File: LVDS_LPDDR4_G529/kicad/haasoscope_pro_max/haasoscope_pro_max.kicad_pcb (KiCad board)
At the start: 10 copper layers, 200 x 125 mm, 4 parts, among them IC1 ADC12DL500ACF, U1 Ti90G529_Functions, U2 MT53E256M32D2DS-046 IT:B, U3 FT601Q

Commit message: Aligned schematics, sort of
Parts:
- IC1: value ADC12DL500ACF -> ADC12DL500ACF_Aligned
- U1: value Ti90G529_Functions -> MT53D512M16D1DS_Aligned; footprint G529:BGA-529_23x23_19.0x19.0mm -> MT53D512M32D2DS-053 WT_D:IC_MT53D512M16D1DS-046_WT_D
- U2: value MT53E256M32D2DS-046 IT:B -> FT601Q_Aligned; footprint MT53D512M32D2DS-053 WT_D:IC_MT53D512M16D1DS-046_WT_D -> Package_DFN_QFN:QFN-76-1EP_9x9mm_P0.4mm_EP5.81x6.31mm
- U3: value FT601Q -> Ti90G529_Functions; footprint Package_DFN_QFN:QFN-76-1EP_9x9mm_P0.4mm_EP5.81x6.31mm -> G529:BGA-529_23x23_19.0x19.0mm
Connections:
- IC1 pad A16: unconnected-(IC1-DGND_2-PadA16) -> (no net)
- IC1 pad A2: unconnected-(IC1-AGND_2-PadA2) -> (no net)
- IC1 pad A3: unconnected-(IC1-AGND_3-PadA3) -> (no net)
- IC1 pad A6: unconnected-(IC1-AGND_4-PadA6) -> (no net)
- IC1 pad A7: unconnected-(IC1-AGND_5-PadA7) -> (no net)
- IC1 pad B3: unconnected-(IC1-AGND_6-PadB3) -> (no net)
- IC1 pad B4: unconnected-(IC1-AGND_7-PadB4) -> (no net)
- IC1 pad B5: unconnected-(IC1-AGND_8-PadB5) -> (no net)
- IC1 pad B6: unconnected-(IC1-AGND_9-PadB6) -> (no net)
- IC1 pad B7: unconnected-(IC1-AGND_10-PadB7) -> (no net)
- IC1 pad C1: unconnected-(IC1-AGND_11-PadC1) -> (no net)
- IC1 pad C2: unconnected-(IC1-AGND_12-PadC2) -> (no net)
- IC1 pad C3: unconnected-(IC1-AGND_13-PadC3) -> (no net)
- IC1 pad C4: unconnected-(IC1-AGND_14-PadC4) -> (no net)
- IC1 pad C5: unconnected-(IC1-AGND_15-PadC5) -> (no net)
- IC1 pad C6: unconnected-(IC1-AGND_16-PadC6) -> (no net)
- IC1 pad C7: unconnected-(IC1-AGND_17-PadC7) -> (no net)
- IC1 pad D3: unconnected-(IC1-AGND_18-PadD3) -> (no net)
- IC1 pad D4: unconnected-(IC1-AGND_19-PadD4) -> (no net)
- IC1 pad D5: unconnected-(IC1-AGND_20-PadD5) -> (no net)
- IC1 pad D6: unconnected-(IC1-AGND_21-PadD6) -> (no net)
- IC1 pad D7: unconnected-(IC1-DGND_3-PadD7) -> (no net)
- IC1 pad E3: unconnected-(IC1-AGND_22-PadE3) -> (no net)
- IC1 pad E5: unconnected-(IC1-VA11_2-PadE5) -> (no net)
- IC1 pad E6: unconnected-(IC1-VA11_3-PadE6) -> (no net)
- IC1 pad E7: unconnected-(IC1-DGND_4-PadE7) -> (no net)
- IC1 pad F1: unconnected-(IC1-AGND_23-PadF1) -> (no net)
- IC1 pad F2: unconnected-(IC1-AGND_24-PadF2) -> (no net)
- IC1 pad F3: unconnected-(IC1-VA11_4-PadF3) -> (no net)
- IC1 pad F4: unconnected-(IC1-VA11_5-PadF4) -> (no net)
- IC1 pad F5: unconnected-(IC1-VA11_6-PadF5) -> (no net)
- IC1 pad F6: unconnected-(IC1-VA11_7-PadF6) -> (no net)
- IC1 pad F7: unconnected-(IC1-DGND_5-PadF7) -> (no net)
- IC1 pad F8: unconnected-(IC1-VD11_2-PadF8) -> (no net)
- IC1 pad G1: unconnected-(IC1-AGND_25-PadG1) -> (no net)
- IC1 pad G12: unconnected-(IC1-VLVDS_2-PadG12) -> (no net)
- IC1 pad G2: unconnected-(IC1-AGND_26-PadG2) -> (no net)
- IC1 pad G4: unconnected-(IC1-VA19_2-PadG4) -> (no net)
- IC1 pad G5: unconnected-(IC1-VA19_3-PadG5) -> (no net)
- IC1 pad G6: unconnected-(IC1-VA19_4-PadG6) -> (no net)
- IC1 pad G7: unconnected-(IC1-DGND_6-PadG7) -> (no net)
- IC1 pad G8: unconnected-(IC1-VD11_3-PadG8) -> (no net)
- IC1 pad H11: unconnected-(IC1-VLVDS_3-PadH11) -> (no net)
- IC1 pad H12: unconnected-(IC1-VLVDS_4-PadH12) -> (no net)
- IC1 pad H13: unconnected-(IC1-VLVDS_5-PadH13) -> (no net)
- IC1 pad H14: unconnected-(IC1-DGND_9-PadH14) -> (no net)
- IC1 pad H2: unconnected-(IC1-AGND_27-PadH2) -> (no net)
- IC1 pad H3: unconnected-(IC1-VA19_5-PadH3) -> (no net)
- IC1 pad H4: unconnected-(IC1-VA19_6-PadH4) -> (no net)
- IC1 pad H5: unconnected-(IC1-VA19_7-PadH5) -> (no net)
- IC1 pad H6: unconnected-(IC1-VA19_8-PadH6) -> (no net)
- IC1 pad H7: unconnected-(IC1-DGND_7-PadH7) -> (no net)
- IC1 pad H8: unconnected-(IC1-DGND_8-PadH8) -> (no net)
- IC1 pad J11: unconnected-(IC1-VLVDS_6-PadJ11) -> (no net)
- IC1 pad J12: unconnected-(IC1-VLVDS_7-PadJ12) -> (no net)
- IC1 pad J13: unconnected-(IC1-VLVDS_8-PadJ13) -> (no net)
- IC1 pad J14: unconnected-(IC1-DGND_12-PadJ14) -> (no net)
- IC1 pad J2: unconnected-(IC1-AGND_28-PadJ2) -> (no net)
- IC1 pad J3: unconnected-(IC1-VA19_9-PadJ3) -> (no net)
- IC1 pad J4: unconnected-(IC1-VA19_10-PadJ4) -> (no net)
- IC1 pad J5: unconnected-(IC1-VA19_11-PadJ5) -> (no net)
- IC1 pad J6: unconnected-(IC1-VA19_12-PadJ6) -> (no net)
- IC1 pad J7: unconnected-(IC1-DGND_10-PadJ7) -> (no net)
- IC1 pad J8: unconnected-(IC1-DGND_11-PadJ8) -> (no net)
- IC1 pad K1: unconnected-(IC1-AGND_29-PadK1) -> (no net)
- IC1 pad K11: unconnected-(IC1-VLVDS_9-PadK11) -> (no net)
- IC1 pad K12: unconnected-(IC1-VLVDS_10-PadK12) -> (no net)
- IC1 pad K2: unconnected-(IC1-AGND_30-PadK2) -> (no net)
- IC1 pad K3: unconnected-(IC1-VA19_13-PadK3) -> (no net)
- IC1 pad K4: unconnected-(IC1-VA19_14-PadK4) -> (no net)
- IC1 pad K5: unconnected-(IC1-VA19_15-PadK5) -> (no net)
- IC1 pad K6: unconnected-(IC1-VA19_16-PadK6) -> (no net)
- IC1 pad K7: unconnected-(IC1-DGND_13-PadK7) -> (no net)
- IC1 pad K8: unconnected-(IC1-VD11_4-PadK8) -> (no net)
- IC1 pad L1: unconnected-(IC1-AGND_31-PadL1) -> (no net)
- IC1 pad L2: unconnected-(IC1-AGND_32-PadL2) -> (no net)
- IC1 pad L3: unconnected-(IC1-VA11_8-PadL3) -> (no net)
- IC1 pad L4: unconnected-(IC1-VA11_9-PadL4) -> (no net)
- IC1 pad L5: unconnected-(IC1-VA11_10-PadL5) -> (no net)
- IC1 pad L6: unconnected-(IC1-VA11_11-PadL6) -> (no net)
- IC1 pad L7: unconnected-(IC1-DGND_14-PadL7) -> (no net)
- IC1 pad L8: unconnected-(IC1-VD11_5-PadL8) -> (no net)
- IC1 pad M3: unconnected-(IC1-AGND_33-PadM3) -> (no net)
- IC1 pad M4: unconnected-(IC1-VA11_12-PadM4) -> (no net)
- IC1 pad M5: unconnected-(IC1-VA11_13-PadM5) -> (no net)
- IC1 pad M6: unconnected-(IC1-VA11_14-PadM6) -> (no net)
- IC1 pad M7: unconnected-(IC1-DGND_15-PadM7) -> (no net)
- IC1 pad M8: unconnected-(IC1-VD11_6-PadM8) -> (no net)
- IC1 pad N3: unconnected-(IC1-AGND_34-PadN3) -> (no net)
- IC1 pad N4: unconnected-(IC1-AGND_35-PadN4) -> (no net)
- IC1 pad N5: unconnected-(IC1-AGND_36-PadN5) -> (no net)
- IC1 pad N6: unconnected-(IC1-AGND_37-PadN6) -> (no net)
- IC1 pad N7: unconnected-(IC1-DGND_16-PadN7) -> (no net)
- IC1 pad P1: unconnected-(IC1-AGND_38-PadP1) -> (no net)
- IC1 pad P2: unconnected-(IC1-AGND_39-PadP2) -> (no net)
- IC1 pad P3: unconnected-(IC1-AGND_40-PadP3) -> (no net)
- IC1 pad P4: unconnected-(IC1-AGND_41-PadP4) -> (no net)
- IC1 pad P5: unconnected-(IC1-AGND_42-PadP5) -> (no net)
- IC1 pad P6: unconnected-(IC1-AGND_43-PadP6) -> (no net)
- IC1 pad P7: unconnected-(IC1-AGND_44-PadP7) -> (no net)
- IC1 pad R2: unconnected-(IC1-AGND_45-PadR2) -> (no net)
- IC1 pad R3: unconnected-(IC1-AGND_46-PadR3) -> (no net)
- IC1 pad R4: unconnected-(IC1-AGND_47-PadR4) -> (no net)
- IC1 pad R5: unconnected-(IC1-AGND_48-PadR5) -> (no net)
- IC1 pad R6: unconnected-(IC1-AGND_49-PadR6) -> (no net)
- IC1 pad R7: unconnected-(IC1-AGND_50-PadR7) -> (no net)
- IC1 pad T1: unconnected-(IC1-AGND_51-PadT1) -> (no net)
- IC1 pad T15: unconnected-(IC1-DGND_17-PadT15) -> (no net)
- IC1 pad T16: unconnected-(IC1-DGND_18-PadT16) -> (no net)
- IC1 pad T2: unconnected-(IC1-AGND_52-PadT2) -> (no net)
- IC1 pad T3: unconnected-(IC1-AGND_53-PadT3) -> (no net)
- IC1 pad T6: unconnected-(IC1-AGND_54-PadT6) -> (no net)
- IC1 pad T7: unconnected-(IC1-AGND_55-PadT7) -> (no net)
- U1 pad A1: unconnected-(U1N-GND-PadA1) -> (no net)
- U1 pad A10: unconnected-(U1D-ftdi_data[12]-PadA10) -> (no net)
- U1 pad A11: unconnected-(U1D-debugout[11]-PadA11) -> (no net)
- U1 pad A12: unconnected-(U1D-boardout[2]-PadA12) -> (no net)
- U1 pad A2: unconnected-(U1I-lvdsin_trig_N-PadA2) -> (no net)
- U1 pad A4: unconnected-(U1I-GPIOB_P_33_CDI31-PadA4) -> (no net)
- U1 pad A8: unconnected-(U1E-ftdi_data[6]-PadA8) -> (no net)
- U1 pad A9: unconnected-(U1E-debugout[2]-PadA9) -> (no net)
- U1 pad AA1: unconnected-(U1L-DDR_DQ[29]-PadAA1) -> (no net)
- U1 pad AA10: unconnected-(U1L-DDR_DQ[19]-PadAA10) -> (no net)
- U1 pad AA12: unconnected-(U1L-DDR_CKE[0]-PadAA12) -> (no net)
- U1 pad AA3: unconnected-(U1L-DDR_DM[3]-PadAA3) -> (no net)
- U1 pad AA5: unconnected-(U1L-DDR_DQ[27]-PadAA5) -> (no net)
- U1 pad AA8: unconnected-(U1L-DDR_DM[2]-PadAA8) -> (no net)
- U1 pad AB1: unconnected-(U1L-DDR_DQ[28]-PadAB1) -> (no net)
- U1 pad AB10: unconnected-(U1N-VDDQ_PHY-PadAB10) -> (no net)
- U1 pad AB11: unconnected-(U1N-GND-PadAB11) -> (no net)
- U1 pad AB12: unconnected-(U1L-DDR_CK_N-PadAB12) -> (no net)
- U1 pad AB2: unconnected-(U1N-GND-PadAB2) -> (no net)
- U1 pad AB3: unconnected-(U1L-DDR_DQS[3]-PadAB3) -> (no net)
- U1 pad AB4: unconnected-(U1L-DDR_DQ[24]-PadAB4) -> (no net)
- U1 pad AB5: unconnected-(U1N-GND-PadAB5) -> (no net)
- U1 pad AB8: unconnected-(U1L-DDR_DQS[2]-PadAB8) -> (no net)
- U1 pad AB9: unconnected-(U1L-DDR_DQ[16]-PadAB9) -> (no net)
- U1 pad B1: unconnected-(U1I-lvds_rx4_11-PadB1) -> (no net)
- U1 pad B10: unconnected-(U1D-debugout[9]-PadB10) -> (no net)
- U1 pad B12: unconnected-(U1D-ftdi_data[15]-PadB12) -> (no net)
- U1 pad B5: unconnected-(U1M-REF_RES_4A-PadB5) -> (no net)
- U1 pad B8: unconnected-(U1N-VCCIO3C-PadB8) -> (no net)
- U1 pad C1: unconnected-(U1I-lvds_rx4_11_N-PadC1) -> (no net)
- U1 pad C12: unconnected-(U1D-boardout[5]-PadC12) -> (no net)
- U1 pad C5: unconnected-(U1E-ext_clkin-PadC5) -> (no net)
- U1 pad C8: unconnected-(U1E-debugout[0]-PadC8) -> (no net)
- U1 pad D1: unconnected-(U1N-GND-PadD1) -> (no net)
- U1 pad D11: unconnected-(U1D-boardout[0]-PadD11) -> (no net)
- U1 pad D12: unconnected-(U1D-ftdi_data[18]-PadD12) -> (no net)
- U1 pad D2: unconnected-(U1I-lvds_rx4_13-PadD2) -> (no net)
- U1 pad D4: unconnected-(U1N-VCCIO4A-PadD4) -> (no net)
- U1 pad D5: unconnected-(U1I-lvdsin_trig_b-PadD5) -> (no net)
- U1 pad D8: unconnected-(U1E-debugout[1]-PadD8) -> (no net)
- U1 pad D9: unconnected-(U1E-debugout[4]-PadD9) -> (no net)
- U1 pad E1: unconnected-(U1J-lvds_rx3_12-PadE1) -> (no net)
- U1 pad E12: unconnected-(U1D-boardout[3]-PadE12) -> (no net)
- U1 pad E5: unconnected-(U1I-lvdsin_trig_b_N-PadE5) -> (no net)
- U1 pad E8: unconnected-(U1E-ftdi_data[5]-PadE8) -> (no net)
- U1 pad F10: unconnected-(U1D-debugout[8]-PadF10) -> (no net)
- U1 pad F12: unconnected-(U1N-VCCIO3B-PadF12) -> (no net)
- U1 pad F3: unconnected-(U1J-lvds_rx4_5-PadF3) -> (no net)
- U1 pad F5: unconnected-(U1I-exttrigin-PadF5) -> (no net)
- U1 pad F8: unconnected-(U1N-VCCIO33_BR-PadF8) -> (no net)
- U1 pad G1: unconnected-(U1J-lvds_rx_bottom_clkin4-PadG1) -> (no net)
- U1 pad G10: unconnected-(U1N-VCCIO3B-PadG10) -> (no net)
- U1 pad G11: unconnected-(U1D-ftdi_data[14]-PadG11) -> (no net)
- U1 pad G12: unconnected-(U1D-ftdi_data[17]-PadG12) -> (no net)
- U1 pad G3: unconnected-(U1J-lvds_rx4_5_N-PadG3) -> (no net)
- U1 pad G4: unconnected-(U1N-VCCIO4A-PadG4) -> (no net)
- U1 pad G5: unconnected-(U1I-GPIOB_N_34-PadG5) -> (no net)
- U1 pad G8: unconnected-(U1B-ftdi_siwu-PadG8) -> (no net)
- U1 pad G9: unconnected-(U1B-ftdi_resetn-PadG9) -> (no net)
- U1 pad H1: unconnected-(U1N-GND-PadH1) -> (no net)
- U1 pad H12: unconnected-(U1D-boardout[4]-PadH12) -> (no net)
- U1 pad H3: unconnected-(U1J-lvds_rx4_4_N-PadH3) -> (no net)
- U1 pad H5: unconnected-(U1J-lvds_rx4_8-PadH5) -> (no net)
- U1 pad H8: unconnected-(U1B-ftdi_gpio0-PadH8) -> (no net)
- U1 pad J1: unconnected-(U1M-REF_RES_4B-PadJ1) -> (no net)
- U1 pad J10: unconnected-(U1N-GND-PadJ10) -> (no net)
- U1 pad J12: unconnected-(U1N-GND-PadJ12) -> (no net)
- U1 pad J3: unconnected-(U1J-lvds_rx4_2-PadJ3) -> (no net)
- U1 pad J5: unconnected-(U1J-lvds_rx4_8_N-PadJ5) -> (no net)
- U1 pad K10: unconnected-(U1N-VCC-PadK10) -> (no net)
- U1 pad K11: unconnected-(U1N-GND-PadK11) -> (no net)
- U1 pad K12: unconnected-(U1N-VCC-PadK12) -> (no net)
- U1 pad K2: unconnected-(U1N-GND-PadK2) -> (no net)
- U1 pad K3: unconnected-(U1J-lvds_rx4_1_N-PadK3) -> (no net)
- U1 pad K4: unconnected-(U1J-lvds_rx4_7-PadK4) -> (no net)
- U1 pad K5: unconnected-(U1N-GND-PadK5) -> (no net)
- U1 pad K8: unconnected-(U1N-VCCAUX-PadK8) -> (no net)
- U1 pad K9: unconnected-(U1N-GND-PadK9) -> (no net)
- U1 pad N1: unconnected-(U1K-lvds_rx3_8-PadN1) -> (no net)
- U1 pad N10: unconnected-(U1N-GND-PadN10) -> (no net)
- U1 pad N11: unconnected-(U1N-VCC-PadN11) -> (no net)
- U1 pad N12: unconnected-(U1N-GND-PadN12) -> (no net)
- U1 pad N2: unconnected-(U1K-lvds_rx3_8_N-PadN2) -> (no net)
- U1 pad N3: unconnected-(U1K-lvds_rx3_7-PadN3) -> (no net)
- U1 pad N4: unconnected-(U1K-lvds_rx3_9-PadN4) -> (no net)
- U1 pad N5: unconnected-(U1K-lvds_rx3_6-PadN5) -> (no net)
- U1 pad N8: unconnected-(U1N-GND-PadN8) -> (no net)
- U1 pad N9: unconnected-(U1N-VCC-PadN9) -> (no net)
- U1 pad P1: unconnected-(U1K-lvds_rx3_4-PadP1) -> (no net)
- U1 pad P10: unconnected-(U1N-GND-PadP10) -> (no net)
- U1 pad P12: unconnected-(U1N-VDD_PHY-PadP12) -> (no net)
- U1 pad P3: unconnected-(U1K-lvds_rx3_7_N-PadP3) -> (no net)
- U1 pad P5: unconnected-(U1K-lvds_rx3_5-PadP5) -> (no net)
- U1 pad R1: unconnected-(U1K-lvds_rx3_4_N-PadR1) -> (no net)
- U1 pad R12: unconnected-(U1N-GND-PadR12) -> (no net)
- U1 pad R3: unconnected-(U1K-lvds_rx3_2_N-PadR3) -> (no net)
- U1 pad R5: unconnected-(U1K-lvds_rx_bottom_clkin3_N-PadR5) -> (no net)
- U1 pad R8: unconnected-(U1N-VCCAUX-PadR8) -> (no net)
- U1 pad T1: unconnected-(U1N-GND-PadT1) -> (no net)
- U1 pad T10: unconnected-(U1N-VDD_PHY-PadT10) -> (no net)
- U1 pad T12: unconnected-(U1N-VDDQ_CK_PHY-PadT12) -> (no net)
- U1 pad T3: unconnected-(U1A-GPIOL_05_CLK26-PadT3) -> (no net)
- U1 pad T4: unconnected-(U1M-TDO-PadT4) -> (no net)
- U1 pad T5: unconnected-(U1M-TMS-PadT5) -> (no net)
- U1 pad T8: unconnected-(U1N-VCC-PadT8) -> (no net)
- U1 pad T9: unconnected-(U1N-VDD_PHY-PadT9) -> (no net)
- U1 pad U1: unconnected-(U1A-LED[0]-PadU1) -> (no net)
- U1 pad U10: unconnected-(U1N-VDDQX_PHY-PadU10) -> (no net)
- U1 pad U12: unconnected-(U1N-VDDPLL_MCB_TOP_PHY-PadU12) -> (no net)
- U1 pad U3: unconnected-(U1A-GPIOL_02-PadU3) -> (no net)
- U1 pad U5: unconnected-(U1M-TCK-PadU5) -> (no net)
- U1 pad U8: unconnected-(U1N-VCC-PadU8) -> (no net)
- U1 pad V1: unconnected-(U1A-GPIOL_06_CLK27-PadV1) -> (no net)
- U1 pad V12: unconnected-(U1N-VDDQX_PHY-PadV12) -> (no net)
- U1 pad V5: unconnected-(U1A-GPIOL_21-PadV5) -> (no net)
- U1 pad V8: unconnected-(U1L-DDR_CAL-PadV8) -> (no net)
- U1 pad W1: unconnected-(U1A-LED[1]-PadW1) -> (no net)
- U1 pad W10: (no net) -> unconnected-(U1B-DQS1_t_B-PadW10)
- U1 pad W12: unconnected-(U1N-VDDQ_PHY-PadW12) -> (no net)
- U1 pad W2: unconnected-(U1A-fan_out-PadW2) -> (no net)
- U1 pad W4: unconnected-(U1A-main_pllin-PadW4) -> (no net)
- U1 pad W5: unconnected-(U1A-GPIOL_03_CLK24-PadW5) -> (no net)
- U1 pad W8: unconnected-(U1L-DDR_A[4]-PadW8) -> (no net)
- U1 pad W9: unconnected-(U1L-DDR_A[3]-PadW9) -> (no net)
- U1 pad Y1: unconnected-(U1N-VDDQ_PHY-PadY1) -> (no net)
- U1 pad Y12: unconnected-(U1N-GND-PadY12) -> (no net)
- U1 pad Y5: unconnected-(U1N-VDDQ_PHY-PadY5) -> (no net)
- U1 pad Y8: unconnected-(U1N-GND-PadY8) -> (no net)
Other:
- board text added: "ADC12DL"
- board text added: "FT601"
- board text added: "MT53D512M32D2DS"
- board text added: "Ti90G529"

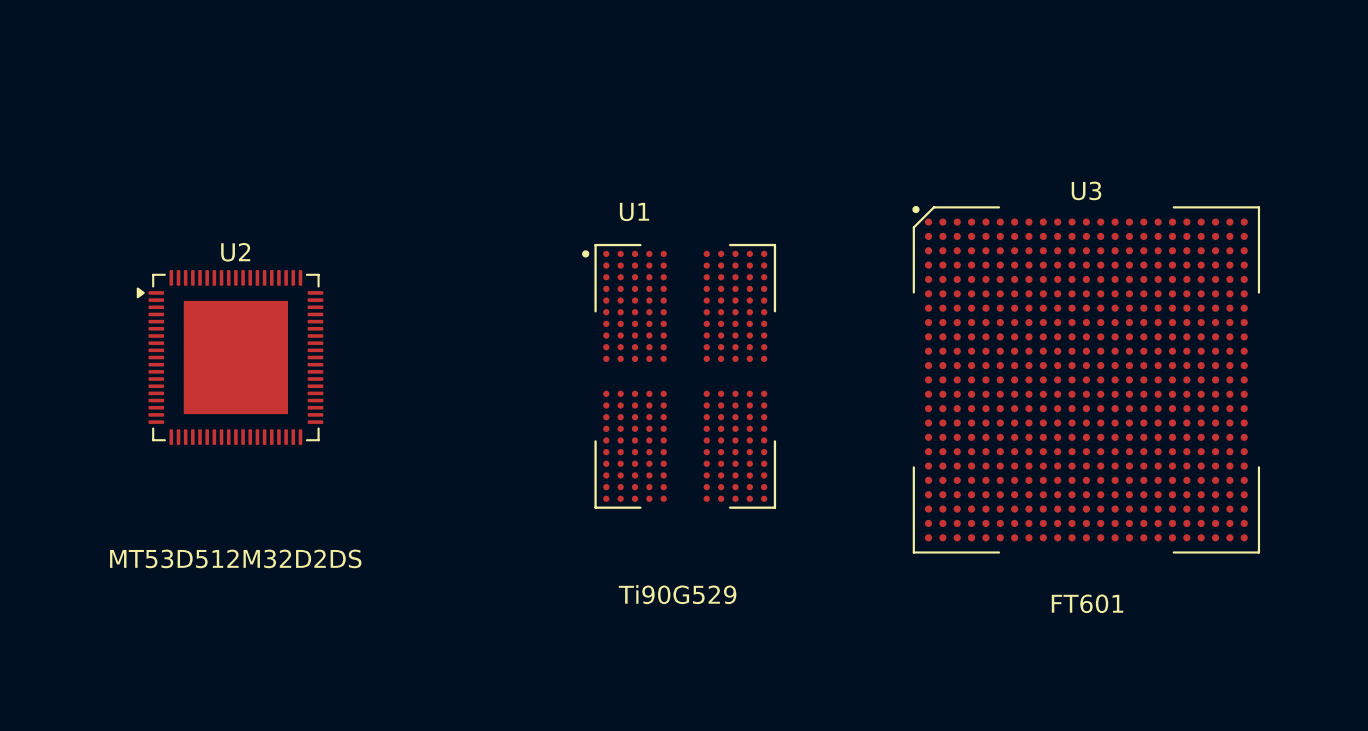
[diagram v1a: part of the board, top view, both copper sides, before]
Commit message: Aligned schematics, connected some components
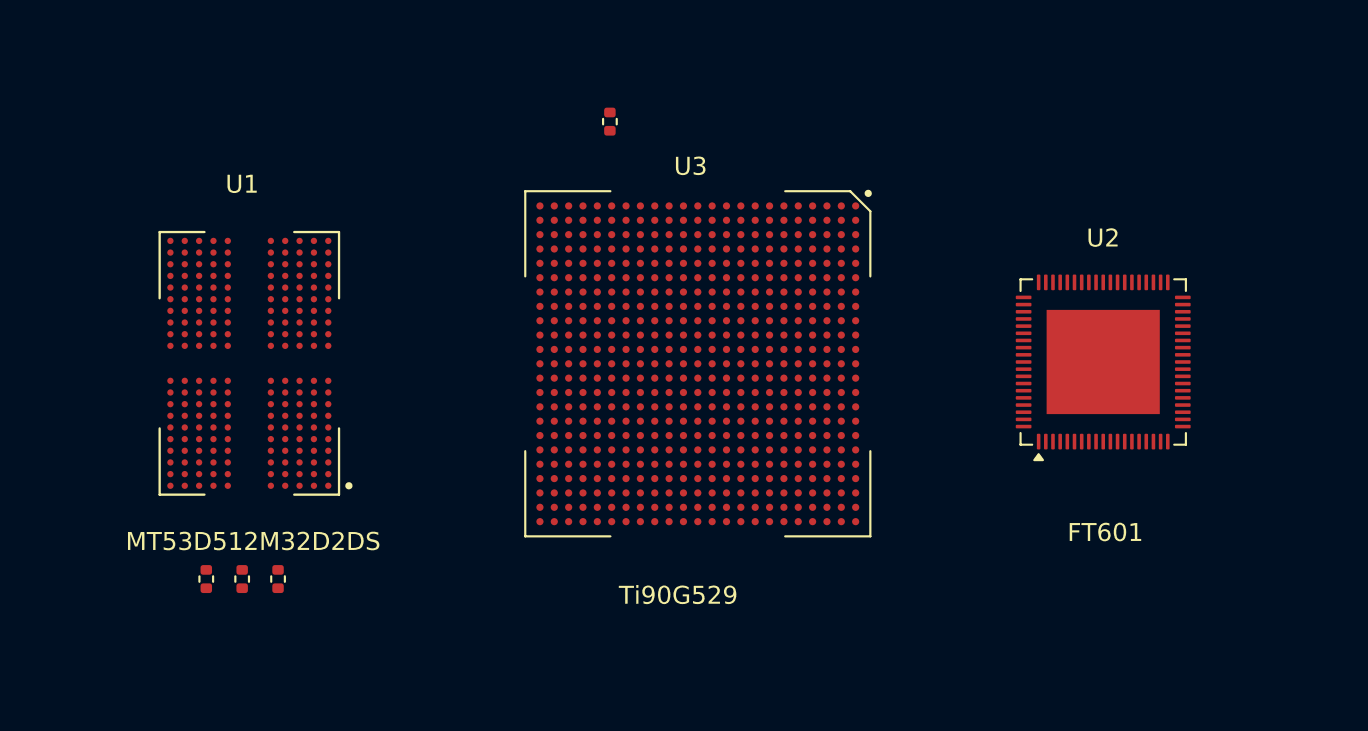
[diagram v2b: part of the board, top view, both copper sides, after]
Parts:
- added R1: 240, Resistor_SMD:R_0402_1005Metric, F.Cu at (190.5, 89.5)
- added R2: 240, Resistor_SMD:R_0402_1005Metric, F.Cu at (172.0, 115.0)
- added R3: 240, Resistor_SMD:R_0402_1005Metric, F.Cu at (170.0, 115.0)
- added R4: 240, Resistor_SMD:R_0402_1005Metric, F.Cu at (168.0, 115.0)
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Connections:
- IC1 pad A10: unconnected-(IC1A-DA0--PadA10) -> Net-(IC1A-DA0-)
- IC1 pad A11: unconnected-(IC1A-DA6+-PadA11) -> Net-(IC1A-DA6+)
- IC1 pad A12: unconnected-(IC1A-DA6--PadA12) -> Net-(IC1A-DA6-)
- IC1 pad A13: unconnected-(IC1A-DC0+-PadA13) -> Net-(IC1A-DC0+)
- IC1 pad A14: unconnected-(IC1A-DC0--PadA14) -> Net-(IC1A-DC0-)
- IC1 pad A16: (no net) -> unconnected-(IC1F-DGND_2-PadA16)
- IC1 pad A2: (no net) -> unconnected-(IC1F-AGND_2-PadA2)
- IC1 pad A3: (no net) -> unconnected-(IC1F-AGND_3-PadA3)
- IC1 pad A6: (no net) -> unconnected-(IC1F-AGND_4-PadA6)
- IC1 pad A7: (no net) -> unconnected-(IC1F-AGND_5-PadA7)
- IC1 pad A9: unconnected-(IC1A-DA0+-PadA9) -> Net-(IC1A-DA0+)
- IC1 pad B10: unconnected-(IC1A-DA1--PadB10) -> Net-(IC1A-DA1-)
- IC1 pad B11: unconnected-(IC1A-DA7+-PadB11) -> Net-(IC1A-DA7+)
- IC1 pad B12: unconnected-(IC1A-DA7--PadB12) -> Net-(IC1A-DA7-)
- IC1 pad B13: unconnected-(IC1A-DC1+-PadB13) -> Net-(IC1A-DC1+)
- IC1 pad B14: unconnected-(IC1A-DC1--PadB14) -> Net-(IC1A-DC1-)
- IC1 pad B15: unconnected-(IC1A-DC7+-PadB15) -> Net-(IC1A-DC7+)
- IC1 pad B16: unconnected-(IC1A-DC7--PadB16) -> Net-(IC1A-DC7-)
- IC1 pad B3: (no net) -> unconnected-(IC1F-AGND_6-PadB3)
- IC1 pad B4: (no net) -> unconnected-(IC1F-AGND_7-PadB4)
- IC1 pad B5: (no net) -> unconnected-(IC1F-AGND_8-PadB5)
- IC1 pad B6: (no net) -> unconnected-(IC1F-AGND_9-PadB6)
- IC1 pad B7: (no net) -> unconnected-(IC1F-AGND_10-PadB7)
- IC1 pad B9: unconnected-(IC1A-DA1+-PadB9) -> Net-(IC1A-DA1+)
- IC1 pad C1: (no net) -> unconnected-(IC1F-AGND_11-PadC1)
- IC1 pad C10: unconnected-(IC1A-DA2--PadC10) -> Net-(IC1A-DA2-)
- IC1 pad C11: unconnected-(IC1A-DA8+-PadC11) -> Net-(IC1A-DA8+)
- IC1 pad C12: unconnected-(IC1A-DA8--PadC12) -> Net-(IC1A-DA8-)
- IC1 pad C13: unconnected-(IC1A-DC2+-PadC13) -> Net-(IC1A-DC2+)
- IC1 pad C14: unconnected-(IC1A-DC2--PadC14) -> Net-(IC1A-DC2-)
- IC1 pad C15: unconnected-(IC1A-DC8+-PadC15) -> Net-(IC1A-DC8+)
- IC1 pad C16: unconnected-(IC1A-DC8--PadC16) -> Net-(IC1A-DC8-)
- IC1 pad C2: (no net) -> unconnected-(IC1F-AGND_12-PadC2)
- IC1 pad C3: (no net) -> unconnected-(IC1F-AGND_13-PadC3)
- IC1 pad C4: (no net) -> unconnected-(IC1F-AGND_14-PadC4)
- IC1 pad C5: (no net) -> unconnected-(IC1F-AGND_15-PadC5)
- IC1 pad C6: (no net) -> unconnected-(IC1F-AGND_16-PadC6)
- IC1 pad C7: (no net) -> unconnected-(IC1F-AGND_17-PadC7)
- IC1 pad C9: unconnected-(IC1A-DA2+-PadC9) -> Net-(IC1A-DA2+)
- IC1 pad D10: unconnected-(IC1A-DA3--PadD10) -> Net-(IC1A-DA3-)
- IC1 pad D11: unconnected-(IC1A-DA9+-PadD11) -> Net-(IC1A-DA9+)
- IC1 pad D12: unconnected-(IC1A-DA9--PadD12) -> Net-(IC1A-DA9-)
- IC1 pad D13: unconnected-(IC1A-DC3+-PadD13) -> Net-(IC1A-DC3+)
- IC1 pad D14: unconnected-(IC1A-DC3--PadD14) -> Net-(IC1A-DC3-)
- IC1 pad D15: unconnected-(IC1A-DC9+-PadD15) -> Net-(IC1A-DC9+)
- IC1 pad D16: unconnected-(IC1A-DC9--PadD16) -> Net-(IC1A-DC9-)
- IC1 pad D3: (no net) -> unconnected-(IC1F-AGND_18-PadD3)
- IC1 pad D4: (no net) -> unconnected-(IC1F-AGND_19-PadD4)
- IC1 pad D5: (no net) -> unconnected-(IC1F-AGND_20-PadD5)
- IC1 pad D6: (no net) -> unconnected-(IC1F-AGND_21-PadD6)
- IC1 pad D7: (no net) -> unconnected-(IC1F-DGND_3-PadD7)
- IC1 pad D9: unconnected-(IC1A-DA3+-PadD9) -> Net-(IC1A-DA3+)
- IC1 pad E10: unconnected-(IC1A-DA4--PadE10) -> Net-(IC1A-DA4-)
- IC1 pad E11: unconnected-(IC1A-DA10+-PadE11) -> Net-(IC1A-DA10+)
- IC1 pad E12: unconnected-(IC1A-DA10--PadE12) -> Net-(IC1A-DA10-)
- IC1 pad E13: unconnected-(IC1A-DC4+-PadE13) -> Net-(IC1A-DC4+)
- IC1 pad E14: unconnected-(IC1A-DC4--PadE14) -> Net-(IC1A-DC4-)
- IC1 pad E15: unconnected-(IC1A-DC10+-PadE15) -> Net-(IC1A-DC10+)
- IC1 pad E16: unconnected-(IC1A-DC10--PadE16) -> Net-(IC1A-DC10-)
- IC1 pad E3: (no net) -> unconnected-(IC1F-AGND_22-PadE3)
- IC1 pad E5: (no net) -> unconnected-(IC1F-VA11_2-PadE5)
- IC1 pad E6: (no net) -> unconnected-(IC1F-VA11_3-PadE6)
- IC1 pad E7: (no net) -> unconnected-(IC1F-DGND_4-PadE7)
- IC1 pad E9: unconnected-(IC1A-DA4+-PadE9) -> Net-(IC1A-DA4+)
- IC1 pad F1: (no net) -> unconnected-(IC1F-AGND_23-PadF1)
- IC1 pad F10: unconnected-(IC1A-DA5--PadF10) -> Net-(IC1A-DA5-)
- IC1 pad F11: unconnected-(IC1A-DA11+-PadF11) -> Net-(IC1A-DA11+)
- IC1 pad F12: unconnected-(IC1A-DA11--PadF12) -> Net-(IC1A-DA11-)
- IC1 pad F13: unconnected-(IC1A-DC5+-PadF13) -> Net-(IC1A-DC5+)
- IC1 pad F14: unconnected-(IC1A-DC5--PadF14) -> Net-(IC1A-DC5-)
- IC1 pad F15: unconnected-(IC1A-DC11+-PadF15) -> Net-(IC1A-DC11+)
- IC1 pad F16: unconnected-(IC1A-DC11--PadF16) -> Net-(IC1A-DC11-)
- IC1 pad F2: (no net) -> unconnected-(IC1F-AGND_24-PadF2)
- IC1 pad F3: (no net) -> unconnected-(IC1F-VA11_4-PadF3)
- IC1 pad F4: (no net) -> unconnected-(IC1F-VA11_5-PadF4)
- IC1 pad F5: (no net) -> unconnected-(IC1F-VA11_6-PadF5)
- IC1 pad F6: (no net) -> unconnected-(IC1F-VA11_7-PadF6)
- IC1 pad F7: (no net) -> unconnected-(IC1F-DGND_5-PadF7)
- IC1 pad F8: (no net) -> unconnected-(IC1F-VD11_2-PadF8)
- IC1 pad F9: unconnected-(IC1A-DA5+-PadF9) -> Net-(IC1A-DA5+)
- IC1 pad G1: (no net) -> unconnected-(IC1F-AGND_25-PadG1)
- IC1 pad G10: unconnected-(IC1A-DACLK--PadG10) -> Net-(IC1C-DACLK-)
- IC1 pad G12: (no net) -> unconnected-(IC1F-VLVDS_2-PadG12)
- IC1 pad G13: unconnected-(IC1A-DC6+-PadG13) -> Net-(IC1A-DC6+)
- IC1 pad G14: unconnected-(IC1A-DC6--PadG14) -> Net-(IC1A-DC6-)
- IC1 pad G15: unconnected-(IC1A-DCCLK+-PadG15) -> Net-(IC1C-DCCLK+)
- IC1 pad G16: unconnected-(IC1A-DCCLK--PadG16) -> Net-(IC1C-DCCLK-)
- IC1 pad G2: (no net) -> unconnected-(IC1F-AGND_26-PadG2)
- IC1 pad G4: (no net) -> unconnected-(IC1F-VA19_2-PadG4)
- IC1 pad G5: (no net) -> unconnected-(IC1F-VA19_3-PadG5)
- IC1 pad G6: (no net) -> unconnected-(IC1F-VA19_4-PadG6)
- IC1 pad G7: (no net) -> unconnected-(IC1F-DGND_6-PadG7)
- IC1 pad G8: (no net) -> unconnected-(IC1F-VD11_3-PadG8)
- IC1 pad G9: unconnected-(IC1A-DACLK+-PadG9) -> Net-(IC1C-DACLK+)
- IC1 pad H10: unconnected-(IC1A-DASTR--PadH10) -> Net-(IC1A-DASTR-)
- IC1 pad H11: (no net) -> unconnected-(IC1F-VLVDS_3-PadH11)
- IC1 pad H12: (no net) -> unconnected-(IC1F-VLVDS_4-PadH12)
- IC1 pad H13: (no net) -> unconnected-(IC1F-VLVDS_5-PadH13)
- IC1 pad H14: (no net) -> unconnected-(IC1F-DGND_9-PadH14)
- IC1 pad H15: unconnected-(IC1A-DCSTR+-PadH15) -> Net-(IC1A-DCSTR+)
- IC1 pad H16: unconnected-(IC1A-DCSTR--PadH16) -> Net-(IC1A-DCSTR-)
- IC1 pad H2: (no net) -> unconnected-(IC1F-AGND_27-PadH2)
- IC1 pad H3: (no net) -> unconnected-(IC1F-VA19_5-PadH3)
- IC1 pad H4: (no net) -> unconnected-(IC1F-VA19_6-PadH4)
- IC1 pad H5: (no net) -> unconnected-(IC1F-VA19_7-PadH5)
- IC1 pad H6: (no net) -> unconnected-(IC1F-VA19_8-PadH6)
- IC1 pad H7: (no net) -> unconnected-(IC1F-DGND_7-PadH7)
- IC1 pad H8: (no net) -> unconnected-(IC1F-DGND_8-PadH8)
- IC1 pad H9: unconnected-(IC1A-DASTR+-PadH9) -> Net-(IC1A-DASTR+)
- IC1 pad J10: unconnected-(IC1B-DBSTR--PadJ10) -> Net-(IC1B-DBSTR-)
- IC1 pad J11: (no net) -> unconnected-(IC1F-VLVDS_6-PadJ11)
- IC1 pad J12: (no net) -> unconnected-(IC1F-VLVDS_7-PadJ12)
- IC1 pad J13: (no net) -> unconnected-(IC1F-VLVDS_8-PadJ13)
- IC1 pad J14: (no net) -> unconnected-(IC1F-DGND_12-PadJ14)
- IC1 pad J15: unconnected-(IC1B-DDSTR+-PadJ15) -> Net-(IC1B-DDSTR+)
- IC1 pad J16: unconnected-(IC1B-DDSTR--PadJ16) -> Net-(IC1B-DDSTR-)
- IC1 pad J2: (no net) -> unconnected-(IC1F-AGND_28-PadJ2)
- IC1 pad J3: (no net) -> unconnected-(IC1F-VA19_9-PadJ3)
- IC1 pad J4: (no net) -> unconnected-(IC1F-VA19_10-PadJ4)
- IC1 pad J5: (no net) -> unconnected-(IC1F-VA19_11-PadJ5)
- IC1 pad J6: (no net) -> unconnected-(IC1F-VA19_12-PadJ6)
- IC1 pad J7: (no net) -> unconnected-(IC1F-DGND_10-PadJ7)
- IC1 pad J8: (no net) -> unconnected-(IC1F-DGND_11-PadJ8)
- IC1 pad J9: unconnected-(IC1B-DBSTR+-PadJ9) -> Net-(IC1B-DBSTR+)
- IC1 pad K1: (no net) -> unconnected-(IC1F-AGND_29-PadK1)
- IC1 pad K10: unconnected-(IC1B-DBCLK--PadK10) -> Net-(IC1C-DBCLK-)
- IC1 pad K11: (no net) -> unconnected-(IC1F-VLVDS_9-PadK11)
- IC1 pad K12: (no net) -> unconnected-(IC1F-VLVDS_10-PadK12)
- IC1 pad K13: unconnected-(IC1B-DD6+-PadK13) -> Net-(IC1B-DD6+)
- IC1 pad K14: unconnected-(IC1B-DD6--PadK14) -> Net-(IC1B-DD6-)
- IC1 pad K15: unconnected-(IC1B-DDCLK+-PadK15) -> Net-(IC1C-DDCLK+)
- IC1 pad K16: unconnected-(IC1B-DDCLK--PadK16) -> Net-(IC1C-DDCLK-)
- IC1 pad K2: (no net) -> unconnected-(IC1F-AGND_30-PadK2)
- IC1 pad K3: (no net) -> unconnected-(IC1F-VA19_13-PadK3)
- IC1 pad K4: (no net) -> unconnected-(IC1F-VA19_14-PadK4)
- IC1 pad K5: (no net) -> unconnected-(IC1F-VA19_15-PadK5)
- IC1 pad K6: (no net) -> unconnected-(IC1F-VA19_16-PadK6)
- IC1 pad K7: (no net) -> unconnected-(IC1F-DGND_13-PadK7)
- IC1 pad K8: (no net) -> unconnected-(IC1F-VD11_4-PadK8)
- IC1 pad K9: unconnected-(IC1B-DBCLK+-PadK9) -> Net-(IC1C-DBCLK+)
- IC1 pad L1: (no net) -> unconnected-(IC1F-AGND_31-PadL1)
- IC1 pad L10: unconnected-(IC1B-DB5--PadL10) -> Net-(IC1B-DB5-)
- IC1 pad L11: unconnected-(IC1B-DB11+-PadL11) -> Net-(IC1B-DB11+)
- IC1 pad L12: unconnected-(IC1B-DB11--PadL12) -> Net-(IC1B-DB11-)
- IC1 pad L13: unconnected-(IC1B-DD5+-PadL13) -> Net-(IC1B-DD5+)
- IC1 pad L14: unconnected-(IC1B-DD5--PadL14) -> Net-(IC1B-DD5-)
- IC1 pad L15: unconnected-(IC1B-DD11+-PadL15) -> Net-(IC1B-DD11+)
- IC1 pad L16: unconnected-(IC1B-DD11--PadL16) -> Net-(IC1B-DD11-)
- IC1 pad L2: (no net) -> unconnected-(IC1F-AGND_32-PadL2)
- IC1 pad L3: (no net) -> unconnected-(IC1F-VA11_8-PadL3)
- IC1 pad L4: (no net) -> unconnected-(IC1F-VA11_9-PadL4)
- IC1 pad L5: (no net) -> unconnected-(IC1F-VA11_10-PadL5)
- IC1 pad L6: (no net) -> unconnected-(IC1F-VA11_11-PadL6)
- IC1 pad L7: (no net) -> unconnected-(IC1F-DGND_14-PadL7)
- IC1 pad L8: (no net) -> unconnected-(IC1F-VD11_5-PadL8)
- IC1 pad L9: unconnected-(IC1B-DB5+-PadL9) -> Net-(IC1B-DB5+)
- IC1 pad M10: unconnected-(IC1B-DB4--PadM10) -> Net-(IC1B-DB4-)
- IC1 pad M11: unconnected-(IC1B-DB10+-PadM11) -> Net-(IC1B-DB10+)
- IC1 pad M12: unconnected-(IC1B-DB10--PadM12) -> Net-(IC1B-DB10-)
- IC1 pad M13: unconnected-(IC1B-DD4+-PadM13) -> Net-(IC1B-DD4+)
- IC1 pad M14: unconnected-(IC1B-DD4--PadM14) -> Net-(IC1B-DD4-)
- IC1 pad M15: unconnected-(IC1B-DD10+-PadM15) -> Net-(IC1B-DD10+)
- IC1 pad M16: unconnected-(IC1B-DD10--PadM16) -> Net-(IC1B-DD10-)
- IC1 pad M3: (no net) -> unconnected-(IC1F-AGND_33-PadM3)
- IC1 pad M4: (no net) -> unconnected-(IC1F-VA11_12-PadM4)
- IC1 pad M5: (no net) -> unconnected-(IC1F-VA11_13-PadM5)
- IC1 pad M6: (no net) -> unconnected-(IC1F-VA11_14-PadM6)
- IC1 pad M7: (no net) -> unconnected-(IC1F-DGND_15-PadM7)
- IC1 pad M8: (no net) -> unconnected-(IC1F-VD11_6-PadM8)
- IC1 pad M9: unconnected-(IC1B-DB4+-PadM9) -> Net-(IC1B-DB4+)
- IC1 pad N10: unconnected-(IC1B-DB3--PadN10) -> Net-(IC1B-DB3-)
- IC1 pad N11: unconnected-(IC1B-DB9+-PadN11) -> Net-(IC1B-DB9+)
- IC1 pad N12: unconnected-(IC1B-DB9--PadN12) -> Net-(IC1B-DB9-)
- IC1 pad N13: unconnected-(IC1B-DD3+-PadN13) -> Net-(IC1B-DD3+)
- IC1 pad N14: unconnected-(IC1B-DD3--PadN14) -> Net-(IC1B-DD3-)
- IC1 pad N15: unconnected-(IC1B-DD9+-PadN15) -> Net-(IC1B-DD9+)
- IC1 pad N16: unconnected-(IC1B-DD9--PadN16) -> Net-(IC1B-DD9-)
- IC1 pad N3: (no net) -> unconnected-(IC1F-AGND_34-PadN3)
- IC1 pad N4: (no net) -> unconnected-(IC1F-AGND_35-PadN4)
- IC1 pad N5: (no net) -> unconnected-(IC1F-AGND_36-PadN5)
- IC1 pad N6: (no net) -> unconnected-(IC1F-AGND_37-PadN6)
- IC1 pad N7: (no net) -> unconnected-(IC1F-DGND_16-PadN7)
- IC1 pad N9: unconnected-(IC1B-DB3+-PadN9) -> Net-(IC1B-DB3+)
- IC1 pad P1: (no net) -> unconnected-(IC1F-AGND_38-PadP1)
- IC1 pad P10: unconnected-(IC1B-DB2--PadP10) -> Net-(IC1B-DB2-)
- IC1 pad P11: unconnected-(IC1B-DB8+-PadP11) -> Net-(IC1B-DB8+)
- IC1 pad P12: unconnected-(IC1B-DB8--PadP12) -> Net-(IC1B-DB8-)
- IC1 pad P13: unconnected-(IC1B-DD2+-PadP13) -> Net-(IC1B-DD2+)
- IC1 pad P14: unconnected-(IC1B-DD2--PadP14) -> Net-(IC1B-DD2-)
- IC1 pad P15: unconnected-(IC1B-DD8+-PadP15) -> Net-(IC1B-DD8+)
- IC1 pad P16: unconnected-(IC1B-DD8--PadP16) -> Net-(IC1B-DD8-)
- IC1 pad P2: (no net) -> unconnected-(IC1F-AGND_39-PadP2)
- IC1 pad P3: (no net) -> unconnected-(IC1F-AGND_40-PadP3)
- IC1 pad P4: (no net) -> unconnected-(IC1F-AGND_41-PadP4)
- IC1 pad P5: (no net) -> unconnected-(IC1F-AGND_42-PadP5)
- IC1 pad P6: (no net) -> unconnected-(IC1F-AGND_43-PadP6)
- IC1 pad P7: (no net) -> unconnected-(IC1F-AGND_44-PadP7)
- IC1 pad P9: unconnected-(IC1B-DB2+-PadP9) -> Net-(IC1B-DB2+)
- IC1 pad R10: unconnected-(IC1B-DB1--PadR10) -> Net-(IC1B-DB1-)
- IC1 pad R11: unconnected-(IC1B-DB7+-PadR11) -> Net-(IC1B-DB7+)
- IC1 pad R12: unconnected-(IC1B-DB7--PadR12) -> Net-(IC1B-DB7-)
- IC1 pad R13: unconnected-(IC1B-DD1+-PadR13) -> Net-(IC1B-DD1+)
- IC1 pad R14: unconnected-(IC1B-DD1--PadR14) -> Net-(IC1B-DD1-)
- IC1 pad R15: unconnected-(IC1B-DD7+-PadR15) -> Net-(IC1B-DD7+)
- IC1 pad R16: unconnected-(IC1B-DD7--PadR16) -> Net-(IC1B-DD7-)
- IC1 pad R2: (no net) -> unconnected-(IC1F-AGND_45-PadR2)
- IC1 pad R3: (no net) -> unconnected-(IC1F-AGND_46-PadR3)
- IC1 pad R4: (no net) -> unconnected-(IC1F-AGND_47-PadR4)
- IC1 pad R5: (no net) -> unconnected-(IC1F-AGND_48-PadR5)
- IC1 pad R6: (no net) -> unconnected-(IC1F-AGND_49-PadR6)
- IC1 pad R7: (no net) -> unconnected-(IC1F-AGND_50-PadR7)
- IC1 pad R9: unconnected-(IC1B-DB1+-PadR9) -> Net-(IC1B-DB1+)
- IC1 pad T1: (no net) -> unconnected-(IC1F-AGND_51-PadT1)
- IC1 pad T10: unconnected-(IC1B-DB0--PadT10) -> Net-(IC1B-DB0-)
- IC1 pad T11: unconnected-(IC1B-DB6+-PadT11) -> Net-(IC1B-DB6+)
- IC1 pad T12: unconnected-(IC1B-DB6--PadT12) -> Net-(IC1B-DB6-)
- IC1 pad T13: unconnected-(IC1B-DD0+-PadT13) -> Net-(IC1B-DD0+)
- IC1 pad T14: unconnected-(IC1B-DD0--PadT14) -> Net-(IC1B-DD0-)
- IC1 pad T15: (no net) -> unconnected-(IC1F-DGND_17-PadT15)
- IC1 pad T16: (no net) -> unconnected-(IC1F-DGND_18-PadT16)
- IC1 pad T2: (no net) -> unconnected-(IC1F-AGND_52-PadT2)
- IC1 pad T3: (no net) -> unconnected-(IC1F-AGND_53-PadT3)
- IC1 pad T6: (no net) -> unconnected-(IC1F-AGND_54-PadT6)
- IC1 pad T7: (no net) -> unconnected-(IC1F-AGND_55-PadT7)
- IC1 pad T9: unconnected-(IC1B-DB0+-PadT9) -> Net-(IC1B-DB0+)
- U1 pad A1: (no net) -> unconnected-(U1E-DNU-PadA1)
- U1 pad A10: (no net) -> unconnected-(U1D-VSS-PadA10)
- U1 pad A11: (no net) -> unconnected-(U1E-DNU-PadA11)
- U1 pad A12: (no net) -> unconnected-(U1E-DNU-PadA12)
- U1 pad A2: (no net) -> unconnected-(U1E-DNU-PadA2)
- U1 pad A4: (no net) -> unconnected-(U1C-VDD2-PadA4)
- U1 pad A5: unconnected-(U1A-ZQ0-PadA5) -> Net-(U1B-ZQ0)
- U1 pad A8: (no net) -> unconnected-(U1E-NC-PadA8)
- U1 pad A9: (no net) -> unconnected-(U1C-VDD2-PadA9)
- U1 pad AA1: (no net) -> unconnected-(U1E-DNU-PadAA1)
- U1 pad AA10: (no net) -> unconnected-(U1C-VDDQ-PadAA10)
- U1 pad AA11: unconnected-(U1B-DQ8_B-PadAA11) -> Net-(U1A-DQ8_B)
- U1 pad AA12: (no net) -> unconnected-(U1E-DNU-PadAA12)
- U1 pad AA2: unconnected-(U1B-DQ0_B-PadAA2) -> Net-(U1A-DQ0_B)
- U1 pad AA3: (no net) -> unconnected-(U1C-VDDQ-PadAA3)
- U1 pad AA4: unconnected-(U1B-DQ7_B-PadAA4) -> Net-(U1A-DQ7_B)
- U1 pad AA5: (no net) -> unconnected-(U1C-VDDQ-PadAA5)
- U1 pad AA8: (no net) -> unconnected-(U1C-VDDQ-PadAA8)
- U1 pad AA9: unconnected-(U1B-DQ15_B-PadAA9) -> Net-(U1A-DQ15_B)
- U1 pad AB1: (no net) -> unconnected-(U1E-DNU-PadAB1)
- U1 pad AB10: (no net) -> unconnected-(U1D-VSS-PadAB10)
- U1 pad AB11: (no net) -> unconnected-(U1E-DNU-PadAB11)
- U1 pad AB12: (no net) -> unconnected-(U1E-DNU-PadAB12)
- U1 pad AB2: (no net) -> unconnected-(U1E-DNU-PadAB2)
- U1 pad AB3: (no net) -> unconnected-(U1D-VSS-PadAB3)
- U1 pad AB4: (no net) -> unconnected-(U1C-VDD2-PadAB4)
- U1 pad AB5: (no net) -> unconnected-(U1D-VSS-PadAB5)
- U1 pad AB8: (no net) -> unconnected-(U1D-VSS-PadAB8)
- U1 pad AB9: (no net) -> unconnected-(U1C-VDD2-PadAB9)
- U1 pad B1: (no net) -> unconnected-(U1E-DNU-PadB1)
- U1 pad B10: (no net) -> unconnected-(U1C-VDDQ-PadB10)
- U1 pad B11: unconnected-(U1B-DQ8_A-PadB11) -> Net-(U1A-DQ8_A)
- U1 pad B12: (no net) -> unconnected-(U1E-DNU-PadB12)
- U1 pad B2: unconnected-(U1B-DQ0_A-PadB2) -> Net-(U1A-DQ0_A)
- U1 pad B4: unconnected-(U1B-DQ7_A-PadB4) -> Net-(U1A-DQ7_A)
- U1 pad B5: (no net) -> unconnected-(U1C-VDDQ-PadB5)
- U1 pad B8: (no net) -> unconnected-(U1C-VDDQ-PadB8)
- U1 pad B9: unconnected-(U1B-DQ15_A-PadB9) -> Net-(U1A-DQ15_A)
- U1 pad C1: (no net) -> unconnected-(U1D-VSS-PadC1)
- U1 pad C10: unconnected-(U1B-DMI1_A-PadC10) -> Net-(U1A-DMI1_A)
- U1 pad C11: unconnected-(U1B-DQ9_A-PadC11) -> Net-(U1A-DQ9_A)
- U1 pad C12: (no net) -> unconnected-(U1D-VSS-PadC12)
- U1 pad C2: unconnected-(U1B-DQ1_A-PadC2) -> Net-(U1A-DQ1_A)
- U1 pad C3: unconnected-(U1B-DMI0_A-PadC3) -> Net-(U1A-DMI0_A)
- U1 pad C4: unconnected-(U1B-DQ6_A-PadC4) -> Net-(U1A-DQ6_A)
- U1 pad C5: (no net) -> unconnected-(U1D-VSS-PadC5)
- U1 pad C8: (no net) -> unconnected-(U1D-VSS-PadC8)
- U1 pad C9: unconnected-(U1B-DQ14_A-PadC9) -> Net-(U1A-DQ14_A)
- U1 pad D1: (no net) -> unconnected-(U1C-VDDQ-PadD1)
- U1 pad D10: unconnected-(U1B-DQS1_t_A-PadD10) -> Net-(U1A-DQS1_t_A)
- U1 pad D11: (no net) -> unconnected-(U1D-VSS-PadD11)
- U1 pad D12: (no net) -> unconnected-(U1C-VDDQ-PadD12)
- U1 pad D2: (no net) -> unconnected-(U1D-VSS-PadD2)
- U1 pad D3: unconnected-(U1B-DQS0_t_A-PadD3) -> Net-(U1A-DQS0_t_A)
- U1 pad D4: (no net) -> unconnected-(U1D-VSS-PadD4)
- U1 pad D5: (no net) -> unconnected-(U1C-VDDQ-PadD5)
- U1 pad D8: (no net) -> unconnected-(U1C-VDDQ-PadD8)
- U1 pad D9: (no net) -> unconnected-(U1D-VSS-PadD9)
- U1 pad E1: (no net) -> unconnected-(U1D-VSS-PadE1)
- U1 pad E10: unconnected-(U1B-DQS1_c_A-PadE10) -> Net-(U1A-DQS1_c_A)
- U1 pad E11: unconnected-(U1B-DQ10_A-PadE11) -> Net-(U1A-DQ10_A)
- U1 pad E12: (no net) -> unconnected-(U1D-VSS-PadE12)
- U1 pad E2: unconnected-(U1B-DQ2_A-PadE2) -> Net-(U1A-DQ2_A)
- U1 pad E3: unconnected-(U1B-DQS0_c_A-PadE3) -> Net-(U1A-DQS0_c_A)
- U1 pad E4: unconnected-(U1B-DQ5_A-PadE4) -> Net-(U1A-DQ5_A)
- U1 pad E5: (no net) -> unconnected-(U1D-VSS-PadE5)
- U1 pad E8: (no net) -> unconnected-(U1D-VSS-PadE8)
- U1 pad E9: unconnected-(U1B-DQ13_A-PadE9) -> Net-(U1A-DQ13_A)
- U1 pad F10: (no net) -> unconnected-(U1C-VDDQ-PadF10)
- U1 pad F11: unconnected-(U1B-DQ11_A-PadF11) -> Net-(U1A-DQ11_A)
- U1 pad F12: (no net) -> unconnected-(U1C-VDD1-PadF12)
- U1 pad F2: unconnected-(U1B-DQ3_A-PadF2) -> Net-(U1A-DQ3_A)
- U1 pad F3: (no net) -> unconnected-(U1C-VDDQ-PadF3)
- U1 pad F4: unconnected-(U1B-DQ4_A-PadF4) -> Net-(U1A-DQ4_A)
- U1 pad F5: (no net) -> unconnected-(U1C-VDD2-PadF5)
- U1 pad F8: (no net) -> unconnected-(U1C-VDD2-PadF8)
- U1 pad F9: unconnected-(U1B-DQ12_A-PadF9) -> Net-(U1A-DQ12_A)
- U1 pad G1: (no net) -> unconnected-(U1D-VSS-PadG1)
- U1 pad G10: (no net) -> unconnected-(U1D-VSS-PadG10)
- U1 pad G11: (no net) -> unconnected-(U1E-NC-PadG11)
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
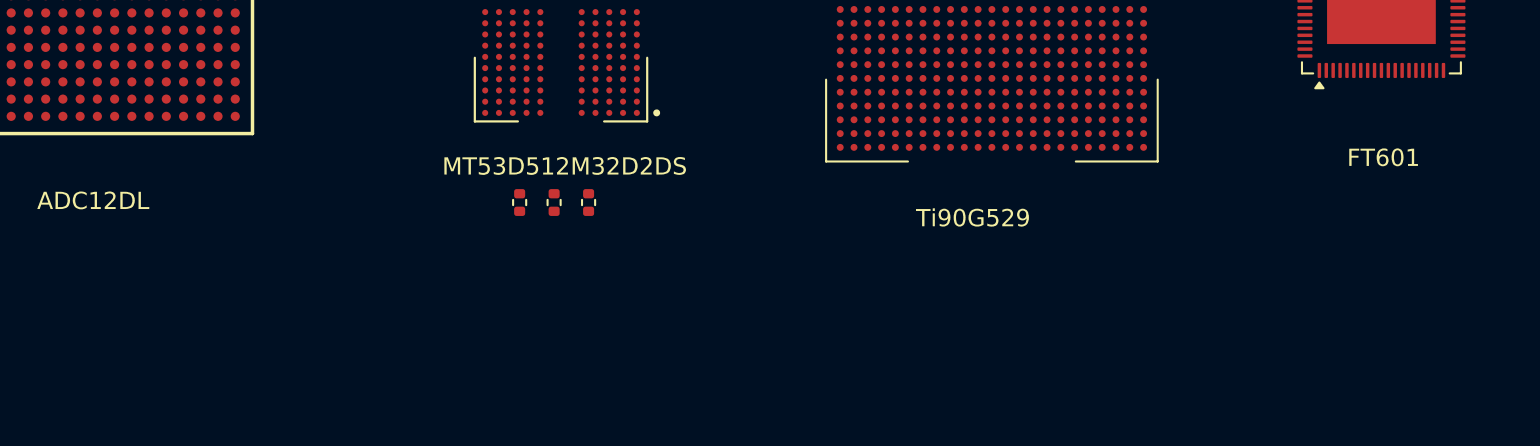
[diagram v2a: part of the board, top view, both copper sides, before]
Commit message: an lvds routed
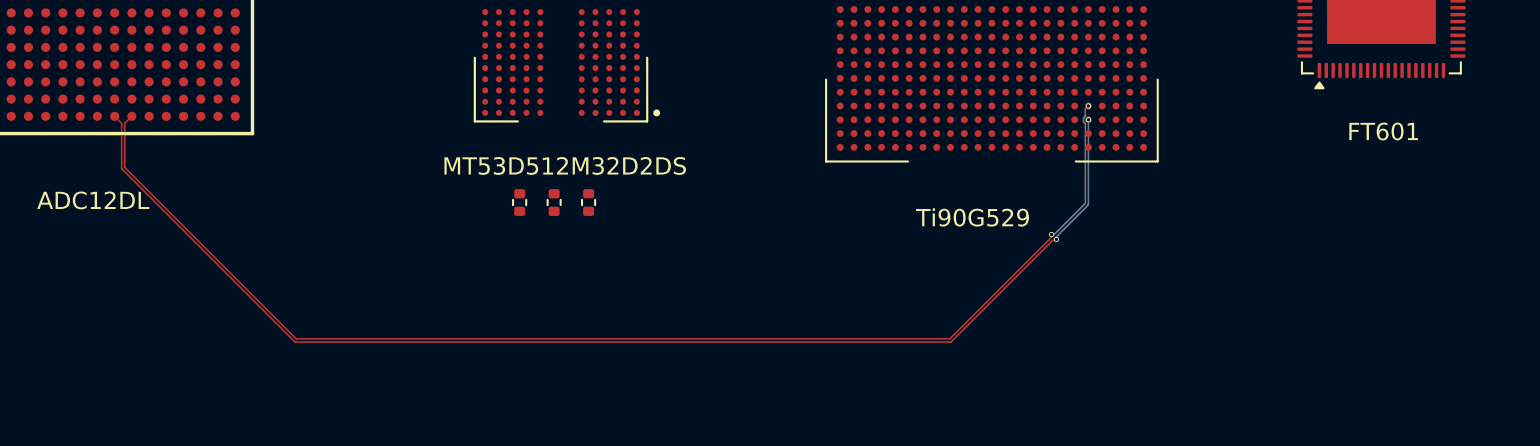
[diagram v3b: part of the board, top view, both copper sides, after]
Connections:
- net Net-(IC1B-DB0+) renamed /fpga_adc/lvds_rx1_1_P
- net Net-(IC1B-DB0-) renamed /fpga_adc/lvds_rx1_1_N
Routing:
- net /fpga_adc/lvds_rx1_1_N: track 0.00 -> 72.1 mm, vias 0 -> 2
- net /fpga_adc/lvds_rx1_1_P: track 0.00 -> 71.8 mm, vias 0 -> 2
- net (no net): vias 0 -> 1

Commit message: 6 NC pads
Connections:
- net Net-(IC1A-DA0+) renamed /fpga_adc/lvds_rx3_1_P
- net Net-(IC1A-DA0-) renamed /fpga_adc/lvds_rx3_1_N
- U3 pad V16: (no net) -> unconnected-(U3J-NC-PadV16)
- U3 pad W10: (no net) -> unconnected-(U3J-NC-PadW10)
- U3 pad W11: (no net) -> unconnected-(U3J-NC-PadW11)
- U3 pad W13: (no net) -> unconnected-(U3J-NC-PadW13)
- U3 pad W14: (no net) -> unconnected-(U3J-NC-PadW14)
- U3 pad W15: (no net) -> unconnected-(U3J-NC-PadW15)
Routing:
- net (no net): vias 1 -> 0
